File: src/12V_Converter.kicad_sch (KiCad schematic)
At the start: 37 parts, among them M4 CSD19534Q5A, M5 NVMFS6H836NLT1G, U2 LM5190RGYR (20V-50V)

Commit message: Update power distribution board
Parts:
- removed C1, C2, C3, C4, C5, C6: 4.7uf, powerDristributionBoard-import-fps:FP-CNA6P-MFG, symbol Altium Content Vault:b4654b650e69147ec39a6b967a45e02
- removed C10, C11, C12, C13, C14, C15, C16, C18, C19, C20, C43, C44, C7, C8, C9: Capacitor 10µF +/-20% 10V 0603, powerDristributionBoard-import-fps:CAPC0603(1608)100_L, symbol Autonomous Vehicle Lab:CAP-NP-2
- removed C17: Capacitor 10 pF +/- 0.25 pF 50 V 0402, powerDristributionBoard-import-fps:CAPC1005X55X30LL05T10, symbol Autonomous Vehicle Lab:CAP-NP-2
- removed C21, C22, C23, C24: 22uf, powerDristributionBoard-import-fps:FP-GRM32E-0_3-0_2-MFG, symbol Altium Content Vault:02cd4be3c70576c341d710602a673aa
- removed R3, R4, R6, R7: 120R3J, powerDristributionBoard-import-fps:RESC0603(1608)_L, symbol Autonomous Vehicle Lab:120R3J
- removed R5: 4D7R5J, powerDristributionBoard-import-fps:RESC0805(2012)_L, symbol Autonomous Vehicle Lab:4D7R5J
- added C1, C2, C3, C4, C5, C6: 4.7uf, Capacitor_SMD:C_1210_3225Metric, symbol Device:C_Small
- added C10, C11, C12, C7, C8, C9: 10nf, Capacitor_SMD:C_0603_1608Metric, symbol Device:C_Small
- added C13: 1uf, Capacitor_SMD:C_0603_1608Metric, symbol Device:C_Small
- added C14: 4.7nf, Capacitor_SMD:C_0603_1608Metric, symbol Device:C_Small
- added C15: 68nf, Capacitor_SMD:C_0603_1608Metric, symbol Device:C_Small
- added C16: 47pf, Capacitor_SMD:C_0603_1608Metric, symbol Device:C_Small
- added C17: 1nf, Capacitor_SMD:C_0402_1005Metric, symbol Device:C_Small
- added C18, C43, C44: 100nf, Capacitor_SMD:C_0603_1608Metric, symbol Device:C_Small
- added C19: 100pf, Capacitor_SMD:C_0603_1608Metric, symbol Device:C_Small
- added C20: 2.2uf, Capacitor_SMD:C_0603_1608Metric, symbol Device:C_Small
- added C21, C22, C23, C24: 22uf, Capacitor_SMD:C_1210_3225Metric, symbol Device:C_Small
- added R2: 59k, Resistor_SMD:R_0603_1608Metric, symbol Device:R_Small_US
- added R3: 9.76k, Resistor_SMD:R_0603_1608Metric, symbol Device:R_Small_US
- added R4: 2.15k, Resistor_SMD:R_0805_2012Metric, symbol Device:R_Small_US
- added R5: 100k, Resistor_SMD:R_0603_1608Metric, symbol Device:R_Small_US
- added R6: 49.9, Resistor_SMD:R_0603_1608Metric, symbol Device:R_Small_US
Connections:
- net GND: now also C1.2, C10.2, C11.2, C12.2, C13.2, C2.2, C20.1, C21.1, C22.1, C23.1, C24.1, C3.2, C4.2, C43.2, C44.2, C5.2, C6.2, C7.2, C8.2, C9.2; no longer Net Tie.2, U2.5 (AGND)
- net LM_Vin: now also C1.1, C10.1, C11.1, C2.1, C3.1, C4.1, C43.1, C44.1, C5.1, C6.1, C7.1, C8.1, C9.1
- net Vout+: now also C13.1, C19.1, C21.2, C22.2, C23.2, C24.2
- net at L1.1, M4.1 (S), M4.2 (S)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: now also C18.2
- net at L1.2, R8.1: now also R6.1
- net at U2.15 (PG): now also R5.2
- net at U2.16 (FPWM_SYNC), U2.4 (FB), U2.7 (VCC): now also C20.2, R5.1
- net at U2.18 (ISNS+): now also C19.2, R6.2
- net at U2.1 (ISET): now also C17.2
- net at U2.13 (CBOOT): now also C18.1
- net at U2.2 (RT): now also R2.2
- net at U2.3 (COMP): now also C16.2, R4.1
- net at U2.6 (IMON_ILIM): now also C14.1, R3.2
- new net: C15.2, R4.2
- new net GNDA: C14.2, C15.1, C16.1, C17.1, Net Tie.2, R2.1, R3.1, U2.5 (AGND)

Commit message: Updated all passive components to KiCad version
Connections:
- net LM_Vin: now also C12.1
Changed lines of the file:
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@@
 		(color 0 0 0 0)
 	)
+	(junction
+		(at 156.21 19.05)
+		(diameter 0)
+		(color 0 0 0 0)
+	)
 	(wire
 		(pts
@@
 	(wire
 		(pts
+			(xy 50.8 58.42) (xy 55.88 58.42)
+		)
+		(stroke
+			(width 0)
+			(type default)
+		)
+	)
+	(wire
+		(pts
 			(xy 22.86 157.48) (xy 27.94 157.48)
 		)
@@
 	(wire
 		(pts
+			(xy 156.21 19.05) (xy 156.21 22.86)
+		)
+		(stroke
+			(width 0)
+			(type default)
+		)
+	)
+	(wire
+		(pts
 			(xy 80.01 31.75) (xy 87.63 31.75)
 		)
@@
 	(wire
 		(pts
+			(xy 156.21 19.05) (xy 158.75 19.05)
+		)
+		(stroke
+			(width 0)
+			(type default)
+		)
+	)
+	(wire
+		(pts
 			(xy 22.86 73.66) (xy 22.86 76.2)
 		)
@@
 	(wire
 		(pts
-			(xy 146.05 19.05) (xy 158.75 19.05)
+			(xy 146.05 19.05) (xy 156.21 19.05)
 		)
 		(stroke
@@
 	(wire
 		(pts
-			(xy 156.21 17.78) (xy 156.21 22.86)
-		)
-		(stroke
-			(width 0)
-			(type default)
-		)
-	)
-	(wire
-		(pts
 			(xy 29.21 19.05) (xy 41.91 19.05)
 		)
@@
 	(wire
 		(pts
-			(xy 51.198 58.42) (xy 55.88 58.42)
-		)
-		(stroke
-			(width 0)
-			(type default)
-		)
-	)
-	(wire
-		(pts
 			(xy 134.62 139.7) (xy 134.62 142.24)
 		)
@@
 			(width 0)
 			(type default)
+		)
+	)
+	(global_label "LM_Vin"
+		(shape input)
+		(at 50.8 58.42 180)
+		(fields_autoplaced yes)
+		(effects
+			(font
+				(size 1.27 1.27)
+			)
+			(justify right)
+		)
+		(property "Intersheetrefs" "${INTERSHEET_REFS}"
+			(at 41.5253 58.42 0)
+			(hide yes)
+			(show_name no)
+			(do_not_autoplace no)
+			(effects
+				(font
+					(size 1.27 1.27)
+				)
+				(justify right)
+			)
+		)
+	)
+	(global_label "LM_Vin"
+		(shape input)
+		(at 158.75 19.05 0)
+		(fields_autoplaced yes)
+		(effects
+			(font
+				(size 1.27 1.27)
+			)
+			(justify left)
+		)
+		(property "Intersheetrefs" "${INTERSHEET_REFS}"
+			(at 168.0247 19.05 0)
+			(hide yes)
+			(show_name no)
+			(do_not_autoplace no)
+			(effects
+				(font
+					(size 1.27 1.27)
+				)
+				(justify left)
+			)
 		)
 	)
@@
 		)
 	)
-	(hierarchical_label "LM_Vin"
-		(shape passive)
-		(at 51.198 58.42 180)
-		(effects
-			(font
-				(size 1.27 1.27)
-			)
-			(justify right)
-		)
-	)
 	(hierarchical_label "Vout+"
 		(shape output)
@@
 		(effects
 			(font
-				(size 1.27 1.27)
-			)
-			(justify left)
-		)
-	)
-	(hierarchical_label "LM_Vin"
-		(shape passive)
-		(at 158.75 19.05 0)
-		(effects
-			(font

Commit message: Tweaked a lot stuff
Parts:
- added U5: LM5190RGYR, EasyEDA:QFN-19_L4.5-W3.5-P0.50-BL-EP_TI_RGY, symbol EasyEDA:LM5190RGYR
- Net Tie1: renamed from Net Tie
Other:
- moved on the sheet: C1, C10, C11, C12, C2, C3, C4, C5, C6, C7, C8, C9

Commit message: Edited the protection circuit
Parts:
- removed U5: LM5190RGYR, EasyEDA:QFN-19_L4.5-W3.5-P0.50-BL-EP_TI_RGY, symbol EasyEDA:LM5190RGYR
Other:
- moved on the sheet: C13, C14, C15, C16, C17, R3

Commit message: Pushing remaining schematic files
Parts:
- removed L1: SMTC1010A-6R8MT, powerDristributionBoard-import-fps:SMTC1010A-6R8MT, symbol Schlib1:SMTC1010A-6R8MT
- removed R8: 5mOhm, powerDristributionBoard-import-fps:CSNL2010, symbol Schlib1:CSNL2010
- removed U2: LM5190RGYR (20V-50V), powerDristributionBoard-import-fps:LM5190RGYR, symbol Schlib1:LM5190RGYR (20V-50V)
- added L1: 6.8uH, symbol Device:L
- added R8: 5mOhms, symbol Device:R_Trim
- added U2: LM5190RGYR_(20V-50V), PowerPCB_Footprints:LM5190RGYR, symbol PowerPCB_Symbols:LM5190RGYR_(20V-50V)
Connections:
- net GND: now also U2.20 (EP), U2.8 (PGND)
- net GNDA: now also U2.5 (AGND)
- net LM_Vin: now also U2.10 (VIN), U2.17 (EN)
- net Vout+: now also R8.2, U2.14 (BIAS), U2.19 (VOUT)
- net at C14.1, R3.2: now also U2.6 (IMON_ILIM)
- net at C18.2, M4.1 (S), M4.2 (S)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: now also L1.1, U2.12 (SW)
- net at R6.1: now also L1.2, R8.1
- net at C20.2, R5.1: now also U2.16 (FPWM_SYNC), U2.4 (FB), U2.7 (VCC)
- net at C18.1: now also U2.13 (CBOOT)
- net at C17.2: now also U2.1 (ISET)
- net at M4.4 (G): now also U2.11 (HO)
- net at R5.2: now also U2.15 (PG)
- net at C19.2, R6.2: now also U2.18 (ISNS+)
- net at R2.2: now also U2.2 (RT)
- net at C16.2, R4.1: now also U2.3 (COMP)
- net at M5.4 (G): now also U2.9 (LO)
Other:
- note added: "CSNL2010"
- note added: "SMTC1010A-6R8MT"

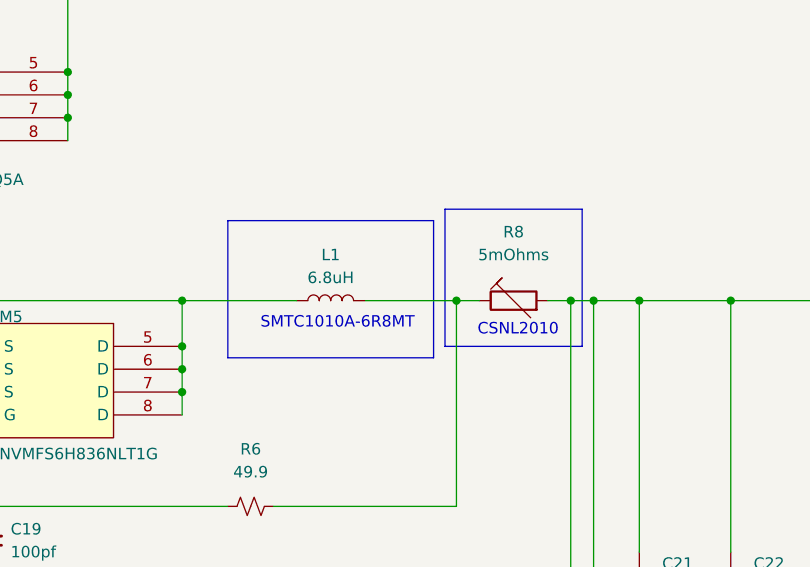
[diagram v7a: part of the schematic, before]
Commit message: Added many footprints
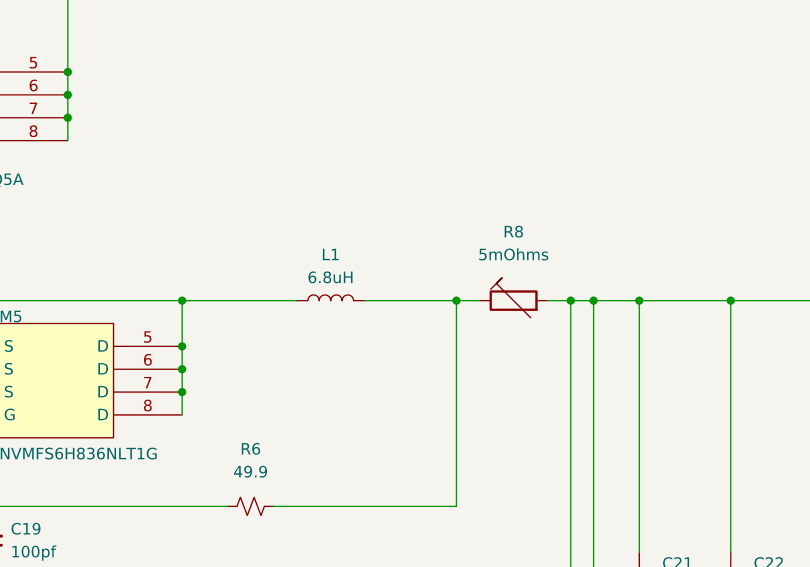
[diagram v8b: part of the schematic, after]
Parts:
- L1: footprint (none) -> PowerPCB_Footprints:SMTC1010A-6R8MT
- M4: footprint powerDristributionBoard-import-fps:DQJ8 -> PowerPCB_Footprints:CSD19534Q5A
- M5: footprint powerDristributionBoard-import-fps:NVMFS6H836NLT1G -> PowerPCB_Footprints:NVMFS6H836NLT1G
- R8: footprint (none) -> PowerPCB_Footprints:CSNL2010
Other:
- note removed: "CSNL2010"
- note removed: "SMTC1010A-6R8MT"
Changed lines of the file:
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@@
 	(generator_version "10.0")
 	(paper "A")
-	(rectangle
-		(start 180.34 87.63)
-		(end 203.2 102.87)
-		(stroke
-			(width 0)
-			(type solid)
-			(color 255 39 32 1)
-		)
-		(fill
-			(type none)
-		)
-	)
-	(rectangle
-		(start 204.47 86.36)
-		(end 219.71 101.6)
-		(stroke
-			(width 0)
-			(type solid)
-			(color 255 39 32 1)
-		)
-		(fill
-			(type none)
-		)
-	)
-	(text "CSNL2010"
-		(exclude_from_sim no)
-		(at 212.598 99.822 0)
-		(effects
-			(font
-				(size 1.27 1.27)
-			)
-		)
-	)
 	(text ""
 		(exclude_from_sim no)
@@
 		)
 	)
-	(text "SMTC1010A-6R8MT"
-		(exclude_from_sim no)
-		(at 192.532 99.06 0)
-		(effects
-			(font
-				(size 1.27 1.27)
-			)
-		)
-	)
 	(junction
 		(at 256.54 96.52)
@@
 			)
 		)
-		(property "Footprint" "powerDristributionBoard-import-fps:DQJ8"
+		(property "Footprint" "PowerPCB_Footprints:CSD19534Q5A"
 			(at 137.16 68.58 0)
 			(hide yes)
@@
 			)
 		)
-		(property "Footprint" ""
+		(property "Footprint" "PowerPCB_Footprints:CSNL2010"
 			(at 212.09 98.298 90)
 			(hide yes)
@@
 			)
 		)
-		(property "Footprint" "powerDristributionBoard-import-fps:NVMFS6H836NLT1G"
+		(property "Footprint" "PowerPCB_Footprints:NVMFS6H836NLT1G"
 			(at 167.64 114.3 0)
 			(hide yes)
@@
 			)
 		)
-		(property "Footprint" ""
+		(property "Footprint" "PowerPCB_Footprints:SMTC1010A-6R8MT"
 			(at 191.77 96.52 0)
 			(hide yes)
